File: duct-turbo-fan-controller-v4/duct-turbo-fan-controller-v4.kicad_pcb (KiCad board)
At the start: 2 copper layers, 42.7 x 48.8 mm, 39 parts, among them J1 Screw_Terminal_01x04, J2 Conn_01x04, J3 USB_OTG, J4 AudioJack4, J7 Conn_01x04, Q1 MMBT3904, Q2 BSS84, SW1 SW_Push, SW2 SW_Push, U1 SCD41-D-R2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

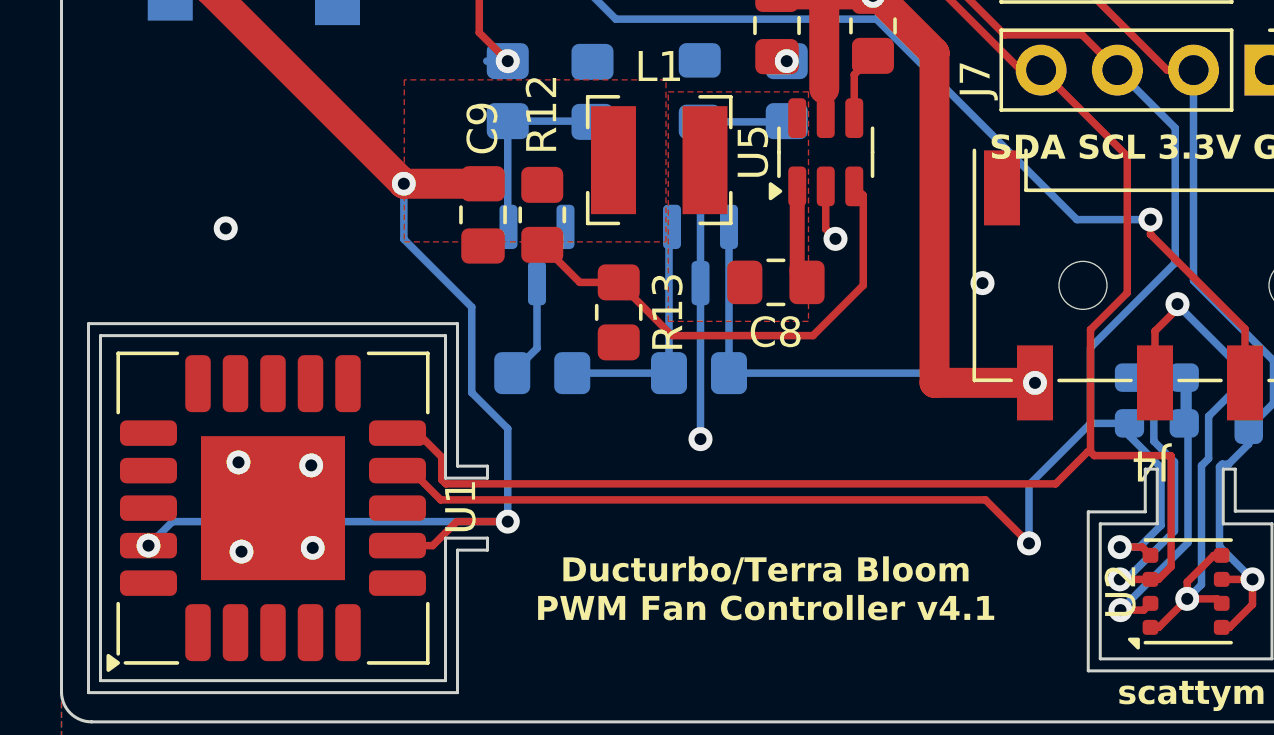
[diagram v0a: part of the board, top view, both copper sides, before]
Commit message: Add missing GND connection for SCD41
Add example esphome home configurations for each board. Not complete.
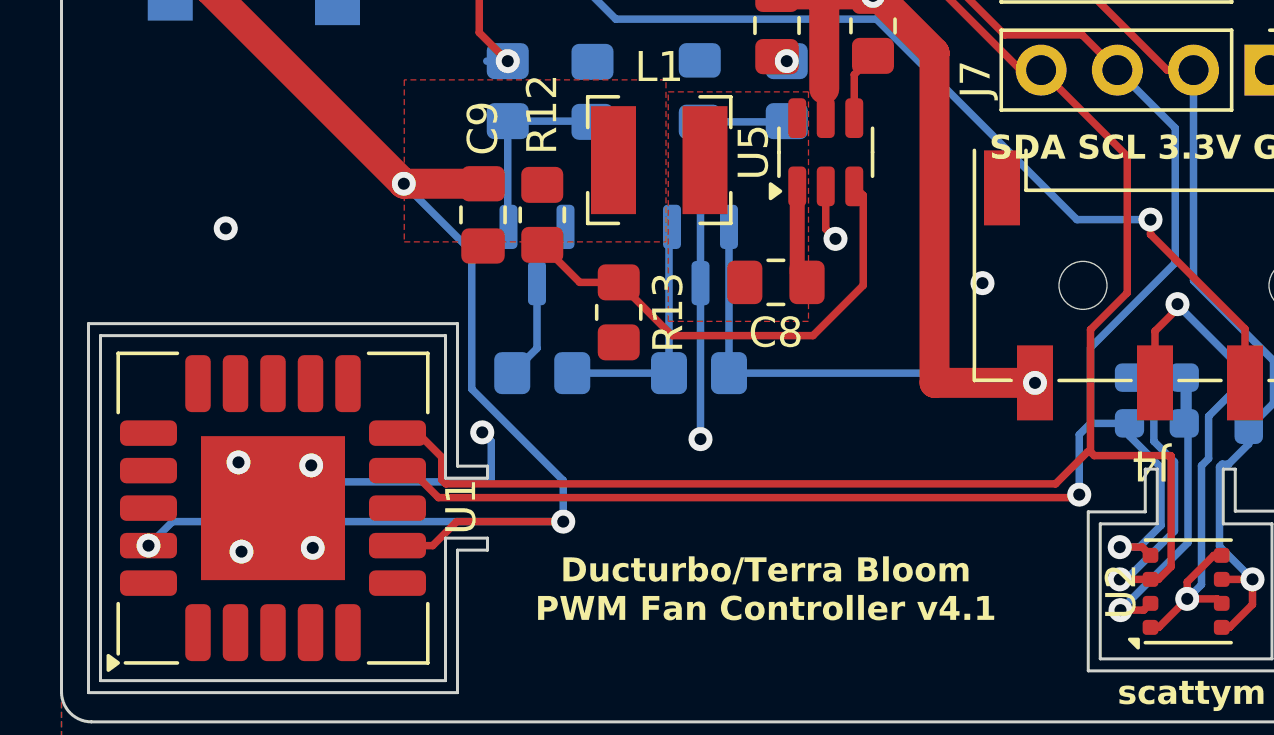
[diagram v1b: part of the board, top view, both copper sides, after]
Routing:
- net GND: track 45.1 -> 53.1 mm, vias 12 -> 13
- net +3V3: track 188.5 -> 193.0 mm
- net BME688_SCL: track 84.5 -> 83.3 mm
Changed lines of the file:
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@@
 		(tags "Bourns SRN4018 SMD inductor")
 		(property "Reference" "L1"
-			(at 0 3.1 360)
+			(at 0 3.1 0)
 			(layer "F.SilkS")
 			(effects
@@
 		)
 		(property "Value" "2.2uH"
-			(at 0 -3.1 360)
+			(at 0 -3.1 0)
 			(layer "F.Fab")
 			(effects
@@
 		)
 		(fp_text user "${REFERENCE}"
-			(at 0 0 360)
+			(at 0 0 0)
 			(layer "F.Fab")
 			(effects
@@
 		(tags "capacitor handsolder")
 		(property "Reference" "C8"
-			(at 0 -1.68 360)
+			(at 0 -1.68 0)
 			(layer "F.SilkS")
 			(effects
@@
 		)
 		(property "Value" "C_Small"
-			(at 0 1.68 360)
+			(at 0 1.68 0)
 			(layer "F.Fab")
 			(effects
@@
 		)
 		(fp_text user "${REFERENCE}"
-			(at 0 0 360)
+			(at 0 0 0)
 			(layer "F.Fab")
 			(effects
@@
 		(tags "resistor handsolder")
 		(property "Reference" "R1"
-			(at 0.035 1.695 360)
+			(at 0.035 1.695 0)
 			(layer "B.SilkS")
 			(effects
@@
 		)
 		(property "Value" "10K"
-			(at 0 -1.65 360)
+			(at 0 -1.65 0)
 			(layer "B.Fab")
 			(effects
@@
 		)
 		(property "Footprint" "Resistor_SMD:R_0805_2012Metric_Pad1.20x1.40mm_HandSolder"
-			(at 0 0 360)
+			(at 0 0 0)
 			(layer "B.Fab")
 			(hide yes)
@@
 		)
 		(property "Datasheet" ""
-			(at 0 0 360)
+			(at 0 0 0)
 			(layer "B.Fab")
 			(hide yes)
@@
 		)
 		(property "Description" ""
-			(at 0 0 360)
+			(at 0 0 0)
 			(layer "B.Fab")
 			(hide yes)
@@
 		)
 		(fp_text user "${REFERENCE}"
-			(at 0 0 360)
+			(at 0 0 0)
 			(layer "B.Fab")
 			(effects
@@
 	)
 	(segment
+		(start 85.591028 87.325)
+		(end 106.85 87.325)
+		(width 0.25)
+		(layer "F.Cu")
+		(net 1)
+	)
+	(segment
 		(start 108.3 88.975)
 		(end 109.05 88.975)
@@
 	)
 	(segment
-		(start 84.691028 86.425)
-		(end 84.225 86.425)
-		(width 0.25)
-		(layer "F.Cu")
-		(net 1)
-	)
-	(segment
 		(start 107.045 71.9)
 		(end 108.22 73.075)
@@
 	)
 	(segment
-		(start 103.825 87.4)
-		(end 85.666028 87.4)
+		(start 84.225 86.425)
+		(end 84.691028 86.425)
 		(width 0.25)
 		(layer "F.Cu")
@@
 	)
 	(segment
+		(start 84.691028 86.425)
+		(end 85.591028 87.325)
+		(width 0.25)
+		(layer "F.Cu")
+		(net 1)
+	)
+	(segment
 		(start 90 66.325)
 		(end 98.886396 66.325)
@@
 	)
 	(segment
-		(start 104.467032 71.9)
-		(end 107.045 71.9)
+		(start 106.85 87.325)
+		(end 106.95 87.225)
 		(width 0.25)
 		(layer "F.Cu")
@@
 	)
 	(segment
-		(start 85.666028 87.4)
-		(end 84.691028 86.425)
+		(start 104.467032 71.9)
+		(end 107.045 71.9)
 		(width 0.25)
 		(layer "F.Cu")
@@
 		(net 1)
 	)
-	(segment
-		(start 105.275 88.85)
-		(end 103.825 87.4)
-		(width 0.25)
-		(layer "F.Cu")
-		(net 1)
-	)
 	(via
-		(at 105.275 88.85)
+		(at 106.95 87.225)
 		(size 0.8)
 		(drill 0.4)
@@
 	(segment
 		(start 107.325 84.85)
-		(end 105.275 86.9)
+		(end 106.95 85.225)
 		(width 0.25)
 		(layer "B.Cu")
@@
 	)
 	(segment
+		(start 106.95 85.225)
+		(end 106.95 87.225)
+		(width 0.25)
+		(layer "B.Cu")
+		(net 1)
+	)
+	(segment
 		(start 108.625 85.273223)
 		(end 109.675 86.323223)
@@
 	)
 	(segment
-		(start 105.275 86.9)
-		(end 105.275 88.85)
-		(width 0.25)
-		(layer "B.Cu")
-		(net 1)
-	)
-	(segment
 		(start 109.675 86.323223)
 		(end 109.675 88.251777)
@@
 	)
 	(via
+		(at 87.05 85.15)
+		(size 0.8)
+		(drill 0.4)
+		(layers "F.Cu" "B.Cu")
+		(net 2)
+	)
+	(via
 		(at 82.35 67.675)
 		(size 0.8)
@@
 	)
 	(segment
+		(start 87.276777 86.8)
+		(end 87.35 86.726777)
+		(width 0.25)
+		(layer "B.Cu")
+		(net 2)
+	)
+	(segment
 		(start 112.6 83.275)
 		(end 110.225 80.9)
@@
 	)
 	(segment
+		(start 81.9 86.8)
+		(end 87.276777 86.8)
+		(width 0.25)
+		(layer "B.Cu")
+		(net 2)
+	)
+	(segment
+		(start 81.35 86.25)
+		(end 81.9 86.8)
+		(width 0.25)
+		(layer "B.Cu")
+		(net 2)
+	)
+	(segment
 		(start 94.325 80.175)
 		(end 94.325 85.374998)
@@
 	)
 	(segment
+		(start 87.35 86.726777)
+		(end 87.35 85.45)
+		(width 0.25)
+		(layer "B.Cu")
+		(net 2)
+	)
+	(segment
 		(start 111.2625 84.6125)
 		(end 111.2625 86.024327)
@@
 	)
 	(segment
+		(start 87.35 85.45)
+		(end 87.05 85.15)
+		(width 0.25)
+		(layer "B.Cu")
+		(net 2)
+	)
+	(segment
 		(start 111.025 90.225)
 		(end 110.55 90.7)
@@
 	)
 	(segment
-		(start 109.881701 73.075)
-		(end 110.76 73.075)
+		(start 86.198223 88.125)
+		(end 89.75 88.125)
 		(width 0.25)
 		(layer "F.Cu")
@@
 	)
 	(segment
-		(start 86.198223 88.125)
-		(end 85.398223 88.925)
+		(start 109.881701 73.075)
+		(end 110.76 73.075)
 		(width 0.25)
 		(layer "F.Cu")
@@
 	)
 	(segment
-		(start 87.9 88.125)
+		(start 85.398223 88.925)
 		(end 86.198223 88.125)
 		(width 0.25)
@@
 	)
 	(segment
-		(start 85.398223 88.925)
-		(end 84.225 88.925)
+		(start 84.225 88.925)
+		(end 85.398223 88.925)
 		(width 0.25)
 		(layer "F.Cu")
@@
 	)
 	(via
-		(at 87.9 88.125)
+		(at 89.75 88.125)
 		(size 0.8)
 		(drill 0.4)
@@
 	)
 	(segment
-		(start 105.68 69.475)
-		(end 105.68 55.885)
+		(start 86.7 79.126346)
+		(end 86.7 83.703984)
 		(width 0.25)
 		(layer "B.Cu")
@@
 	)
 	(segment
-		(start 87.9 85.025)
-		(end 86.7 83.825)
+		(start 105.68 69.475)
+		(end 105.68 55.885)
 		(width 0.25)
 		(layer "B.Cu")
@@
 	)
 	(segment
-		(start 87.9 88.125)
-		(end 76.725 88.125)
+		(start 84.436154 76.8625)
+		(end 86.7 79.126346)
 		(width 0.25)
 		(layer "B.Cu")
@@
 	)
 	(segment
+		(start 86.7 83.703984)
+		(end 89.75 86.753984)
+		(width 0.25)
+		(layer "B.Cu")
+		(net 4)
+	)
+	(segment
 		(start 113.425 84.175)
 		(end 112.6 85)
@@
 	)
 	(segment
-		(start 84.436154 78.711154)
-		(end 84.436154 76.8625)
-		(width 0.25)
-		(layer "B.Cu")
-		(net 4)
-	)
-	(segment
 		(start 103.961778 50.89)
 		(end 110.675 50.89)
@@
 	)
 	(segment
-		(start 87.9 88.125)
-		(end 87.9 85.025)
-		(width 0.25)
-		(layer "B.Cu")
-		(net 4)
-	)
-	(segment
 		(start 110.76 73.075)
 		(end 110.76 80.095424)
@@
 	)
 	(segment
-		(start 85.9 53.3)
-		(end 83.575 53.3)
+		(start 89.75 86.753984)
+		(end 89.75 88.125)
 		(width 0.25)
 		(layer "B.Cu")
@@
 	)
 	(segment
-		(start 76.725 88.125)
-		(end 75.925 88.925)
+		(start 85.9 53.3)
+		(end 83.575 53.3)
 		(width 0.25)
 		(layer "B.Cu")
@@
 	)
 	(segment
-		(start 86.7 80.975)
-		(end 84.436154 78.711154)
-		(width 0.25)
-		(layer "B.Cu")
-		(net 4)
-	)
-	(segment
-		(start 86.7 83.825)
-		(end 86.7 80.975)
+		(start 82.5 56.8)
+		(end 82.5 54.375)
 		(width 0.25)
 		(layer "B.Cu")
@@
 	)
 	(segment
-		(start 82.5 56.8)
-		(end 82.5 54.375)
+		(start 76.725 88.125)
+		(end 89.75 88.125)
 		(width 0.25)
 		(layer "B.Cu")
@@
 		(width 0.25)
 		(layer "B.Cu")
+		(net 4)
+	)
+	(segment
+		(start 75.925 88.925)
+		(end 76.725 88.125)
+		(width 0.25)
+		(layer "B.Cu")

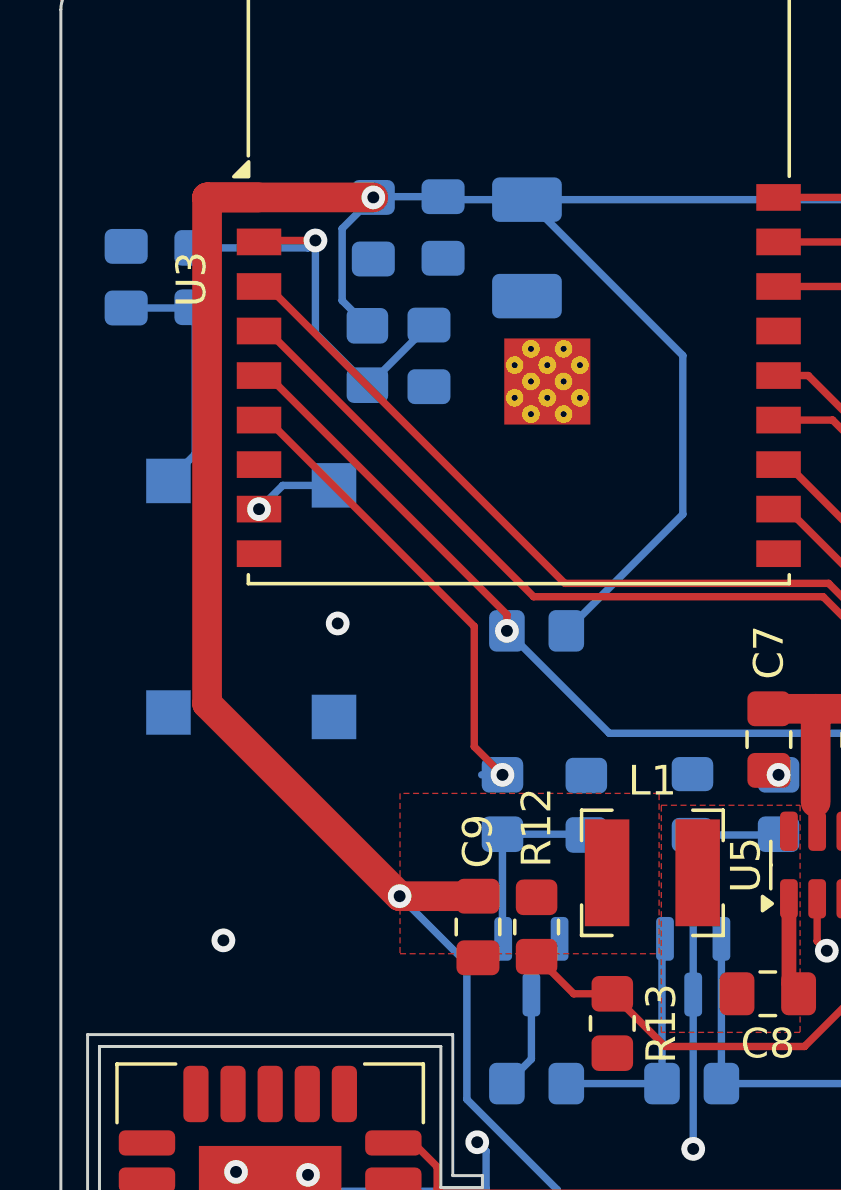
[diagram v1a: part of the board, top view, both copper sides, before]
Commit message: Increase size of 3.3v net to esp32
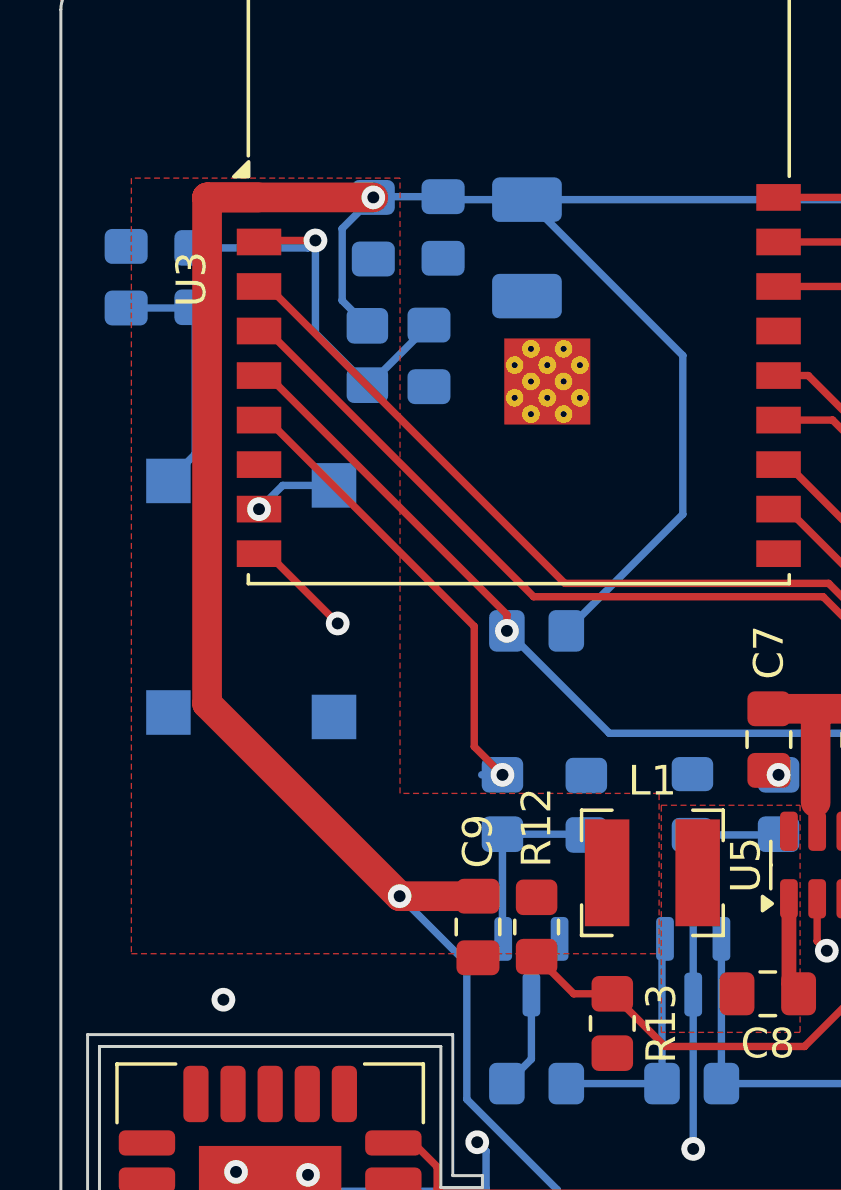
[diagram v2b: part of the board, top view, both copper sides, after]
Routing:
- net GND: track 53.1 -> 56.7 mm
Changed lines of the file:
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@@
+	)
+	(segment
+		(start 79.7 65.325)
+		(end 80 65.325)
+		(width 0.25)
+		(layer "F.Cu")
+		(net 2)
 	)
 	(segment
@@
 	)
 	(segment
+		(start 80 65.325)
+		(end 82.35 67.675)
+		(width 0.25)
+		(layer "F.Cu")
+		(net 2)
+	)
+	(segment
 		(start 111.437501 89.25)
 		(end 111.7 89.25)
@@
 	)
 	(via
-		(at 78.5 78.35)
+		(at 78.5 80.35)
 		(size 0.8)
 		(drill 0.4)
@@
 		(polygon
 			(pts
-				(xy 93.175 73.4) (xy 84.45 73.4) (xy 84.45 78.8) (xy 93.175 78.8)
+				(xy 93.175 73.4) (xy 84.45 73.4) (xy 84.45 52.675) (xy 75.4 52.675) (xy 75.4 78.8) (xy 93.175 78.8)
 			)
 		)

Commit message: New tag for v4 board
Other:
- board text added: "Ducturbo/Terra Bloom PWM Fan Controller v4.2"
- board text removed: "Ducturbo/Terra Bloom PWM Fan Controller v4.1"
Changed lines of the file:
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@@
 		)
 	)
-	(gr_text "Ducturbo/Terra Bloom\nPWM Fan Controller v4.1"
+	(gr_text "Ducturbo/Terra Bloom\nPWM Fan Controller v4.2"
 		(at 96.5 91.5 0)
 		(layer "F.SilkS")

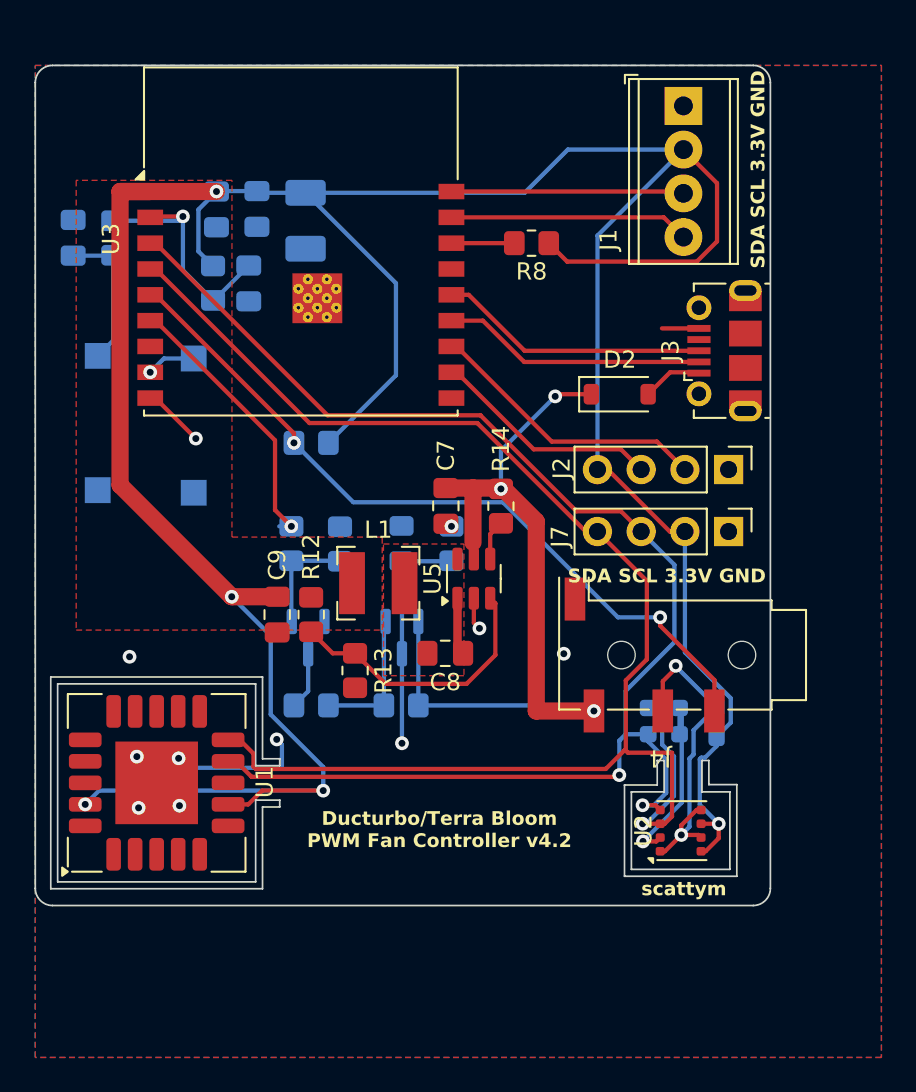
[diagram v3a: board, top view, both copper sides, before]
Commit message: Increase size of cutouts to 0.8mm as per pcbway spec.
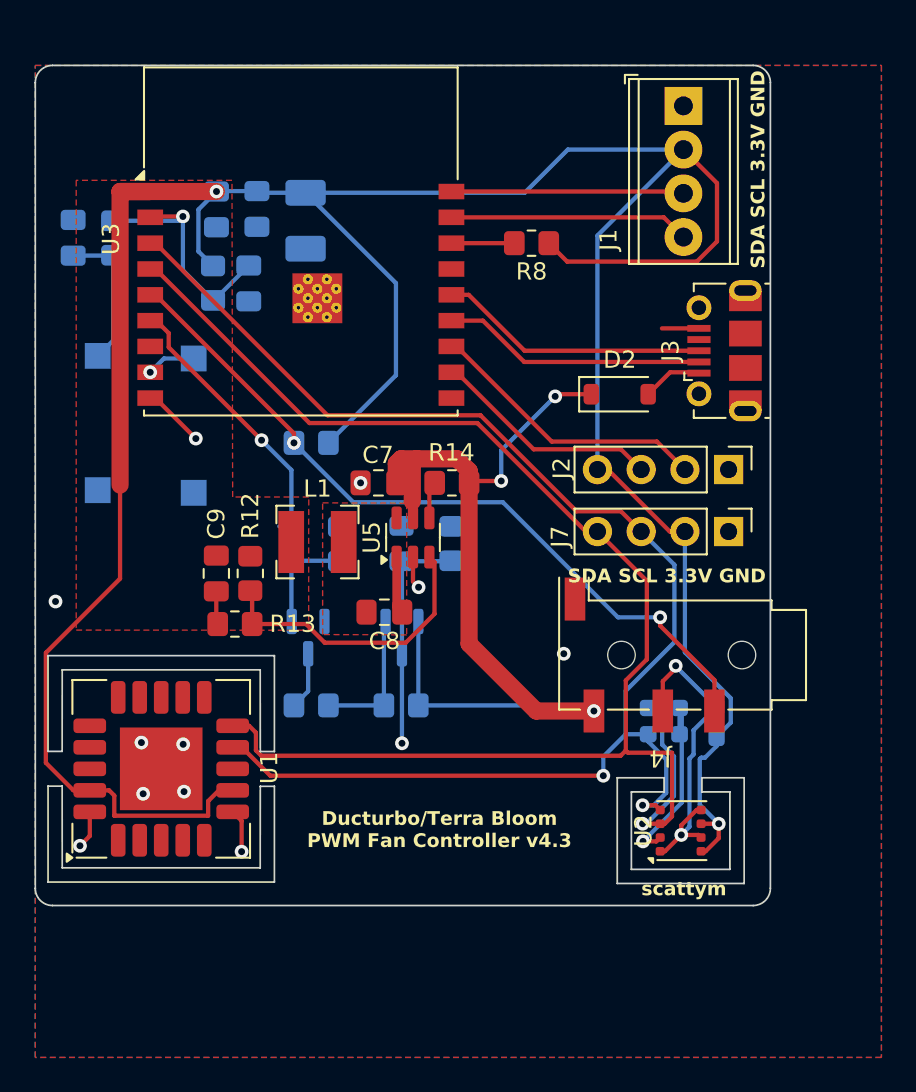
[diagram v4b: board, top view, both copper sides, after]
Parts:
- moved R13 7.48 mm to (84.6, 78.5), turned to 180 degrees
- moved C8 4.27 mm to (93.3, 77.8)
- moved C9 4.27 mm to (83.5, 75.5)
- moved L1 4.27 mm to (89.4, 73.7)
- moved R12 4.27 mm to (85.5, 75.5)
- moved U5 4.27 mm to (95.0, 73.4)
- moved C7 4.14 mm to (93.0, 70.2), turned to 180 degrees
- moved R14 3.15 mm to (97.2, 70.2), turned to 180 degrees
- moved U1 0.86 mm to (80.3, 86.9)
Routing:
- net +3V3: track 193.0 -> 179.5 mm, vias 5 -> 2
- net +10V: track 51.5 -> 53.8 mm
- net GND: track 56.7 -> 55.0 mm, vias 13 -> 14
- net Net-(U5-FB): track 16.1 -> 17.1 mm
- net BME688_SCL: track 83.3 -> 82.8 mm
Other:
- outline, holes or cut-outs redrawn
- board text added: "Ducturbo/Terra Bloom PWM Fan Controller v4.3"
- board text removed: "Ducturbo/Terra Bloom PWM Fan Controller v4.2"
